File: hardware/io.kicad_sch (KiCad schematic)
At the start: 26 parts, among them J3 HALL, J4 I2C, J5 UART, J6 GPIO, J7 SWD, SW2 USER/BOOT

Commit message: Rev 0.2: 内蔵機能 (電流源/シンク・USB-PD・OPA/CMP 全モード) の活用
回路 (102/102 ネット一致):
- USB-PD シンクでモーター電源を供給: F3 → U5 LM74700 + Q10 → VBUS (PC3 で許可),
  USB VBUS 監視 (PA2), SMAJ20A。USBLC6 の基準を +3V3 に変更 (VBUS 20V 対策)
- J1 の逆接保護を U4 LM74700 + Q9 のハイサイド理想ダイオードに変更 (J1 / PD を安全に OR)
- 3 相センシングを PA5/PA6/PA7 に集約 (W 相 PA12 → PA6): CMP3 内部仮想中性点 + TIM2 捕捉
  によるセンサレス BEMF 検出, TIM2 ホール XOR, ISOURCE2 結線診断を同じピンで利用
- JP7: OPA3 入力を HB0 レッグ / バス電流で切替 (CMP2 + DAC でバス過電流・電流制限)
- JP8 + C105: QII1 (OPA1 → CMP1 → TIM3) でタコ / VR センサ / ブラシ DC 電流リップル計数
- 状態 LED を PC4 (USER/BOOT) と共用, J6/J7 を再割当 (1 線 SDI)

ファームウェア (警告 0):
- mpb.h ライブラリ: PD シンク (WCH USBPD_SNK 移植 + 8〜15V ポリシー + 給電パス制御),
  過電流保護 (CMP3/CMP2+DAC, TIM2 停止割込み), BEMF, ホール, タコ, NTC, 結線自己診断, TIM3 時間基準
- ブートローダ / テンプレートの状態 LED を PC4 (オープンドレイン) に変更

ドキュメント: docs/advanced_features.md (検討と判断, 要実機確認事項, Rev 0.3 候補)

Co-Authored-By: Claude Opus 5.5 <noreply@anthropic.com>
Claude-Session: https://claude.ai/code/session_01LENFjjhDfYjJZV1NWhB9uV
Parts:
- removed J4: I2C, Connector_JST:JST_SH_SM04B-SRSS-TB_1x04-1MP_P1.00mm_Horizontal, symbol mdrv:CONN4
- removed J5: UART, Connector_JST:JST_XH_B4B-XH-A_1x04_P2.50mm_Vertical, symbol mdrv:CONN4
- removed J7: SWD, Connector_PinHeader_2.54mm:PinHeader_1x05_P2.54mm_Vertical, symbol mdrv:CONN5
- added C105: 0.1uF, Capacitor_SMD:C_0402_1005Metric, symbol mdrv:C
- added J7: SDI, Connector_PinHeader_2.54mm:PinHeader_1x04_P2.54mm_Vertical, symbol mdrv:CONN4
- added JP8: QII_SRC, Connector_PinHeader_2.54mm:PinHeader_1x03_P2.54mm_Vertical, symbol mdrv:CONN3
- added R114: 4.7k (DNP), Resistor_SMD:R_0402_1005Metric, symbol mdrv:R
- added R123: 4.7k, Resistor_SMD:R_0402_1005Metric, symbol mdrv:R
- D3: renamed from JP6; value LED_EN -> GREEN STAT; footprint Jumper:SolderJumper-2_P1.3mm_Bridged_RoundedPad1.0x1.5mm -> LED_SMD:LED_0603_1608Metric; symbol mdrv:SJ2 -> mdrv:LED; MPN はんだジャンパ (通常ショート) -> (none)
- J4: renamed from D3; value GREEN STAT -> I2C; footprint LED_SMD:LED_0603_1608Metric -> Connector_JST:JST_SH_SM04B-SRSS-TB_1x04-1MP_P1.00mm_Horizontal; symbol mdrv:LED -> mdrv:CONN4; MPN (none) -> JST SH 4P (Qwiic/STEMMA QT 配列)
- J5: renamed from R115; value 4.7k (DNP) -> UART; footprint Resistor_SMD:R_0402_1005Metric -> Connector_JST:JST_XH_B4B-XH-A_1x04_P2.50mm_Vertical; symbol mdrv:R -> mdrv:CONN4; now fitted
- renumbered R114 to R115
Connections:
- net GPIO_PC3 is gone; now on net GPIO_PC4: J6.3 (P3)
- net +3V3: now also D3.2 (A), J4.2 (P2), J5.2 (P2), J7.1 (P1), R114.1; no longer J5.1
- net +5V: now also J6.7 (P7); no longer J6.8 (P8)
- net GND: now also J5.1 (P1), J6.8 (P8), J7.4 (P4)
- net GPIO_PC4: now also R112.2; no longer J6.4 (P4)
- net GPIO_PC5: now also J6.4 (P4); no longer J6.6 (P6)
- net I2C_SCL: now also J4.4 (P4), R115.2; no longer J5.2
- net I2C_SDA: now also J4.3 (P3), R114.2; no longer R115.2
- net SWDIO: now also J7.2 (P2)
- net UART_RX: now also J5.4 (P4)
- net UART_TX: now also J5.3 (P3)
- net nFAULT_IN: now also J6.6 (P6); no longer J6.7 (P7)
- net nRST: now also J7.3 (P3)
- net GPIO_PA6 renamed LED_STAT_K
- net LED_STAT_K: now also R112.1; no longer J6.5 (P5)
- removed net LED_STAT: D3.2, R112.1
- removed net LED_STAT_A: J4.2 (A), R112.2
- new net IBUS_F: JP8.3 (P3)
- new net QII_IN: C105.2
- new net QII_SRC: C105.1, JP8.2 (P2)
- new net TACH_IN: J6.5 (P5), R123.1
- new net TACH_R: JP8.1 (P1), R123.2
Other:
- note added: "(ブラシ DC の整流子リップル計数 = エンコーダ無し位置推定)。OPA1 出力は ADC IN19 でも読める"
- note added: "PC4: GPIO / TIM1_CH2_3 / SPI_MISO (USER/BOOT + 状態 LED 兼用, 例: DIR 入力)"
- note added: "TACH_IN → R123 → JP8 1-2 → C105 → PA12: OPA1 (AV 20/40, 自己バイアス 1.23V) → CMP1 (ヒス 100/200mV)"
- note added: "nFAULT (PA13 = TIM1_BKIN_1): Low で全ゲート OFF。10k プルアップ。3.3V 系 I/O は 5V 非耐性"
- note added: "→ TIM3 CH1 キャプチャ。ファン FG, VR センサ, 小振幅パルスの周期計測。JP8 2-3 はバス電流の AC 成分"
- note added: "汎用 GPIO 引き出し (J6) / QII1 小信号入力 (タコ・VR センサ・電流リップル)"
- note added: "温度検出 (NTC ← ISOURCE1) / USER・BOOT ボタン + 状態 LED (PC4 共用)"
- note added: "状態 LED = PC4 Low で点灯 (USER/BOOT ボタンと共用, ボタン押下中も点灯)。PA6 は 3 相センシング (W) へ。"
- note added: "通信 (I2C / UART) / デバッグ (WCH-LinkE 1 線 SDI)"
- note removed: "3.3V 系 I/O は 5V 非耐性 (絶対最大 VDD33+0.3V)。"
- note removed: "PA6 = 状態 LED。JP6 を切ると PA6 を J6 の汎用 GPIO として使える。"
- note removed: "PA6: GPIO / TIM2_CH2 / ISINK1 (状態 LED 兼用, JP6)"
- note removed: "PC3: GPIO / TIM1_CH1_3 / SPI_MOSI (例: STEP 入力)"
- note removed: "PC4: GPIO / TIM1_CH2_3 / SPI_MISO (USER/BOOT ボタン兼用, 例: DIR 入力)"
- note removed: "nFAULT (PA13 = TIM1_BKIN_1): Low で全ゲート OFF。10k プルアップ"
- note removed: "汎用 GPIO 引き出し (J6)"
- note removed: "温度検出 (パワー段近傍 NTC) / USER・BOOT ボタン / 状態 LED"
- note removed: "通信 (I2C / UART) / デバッグ (WCH-LinkE SDI)"
- moved on the sheet: D3, R112, R115

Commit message: Rev 0.3: パワー段を子基板化 (A/B/C/D) し 2 層基板レイアウトを作成
構成:
- 主基板 (60x42mm, 2 層): 右 = CH32M030 / USB-C / GPIO・I2C・UART・SDI・HALL,
  左上 = 電源 (J1 → F1 → 理想ダイオード, USB-PD 経路), 左下 = 基板間コネクタ J9/J10 (裏面)
- 子基板と裏面同士を背中合わせに重ねる (基板間 約5mm, 裏面部品は高さ 2mm 以下)。
  RESET / USER・BOOT / センシング選択は主基板 TOP、電流チャネル選択 JP5/JP7 は子基板 TOP
- 子基板 A: TPN1R603PL (既存回路) / B: TKR74F04PB (24V 系, 66x66mm) /
  C: MTN2306AN3 (廉価版) / D: MOSFET なし (全信号をピンヘッダへ引き出し)
- 基板間ピンは同じ番号同士が嵌合 (ソケットを 270° 回転して裏面実装, 座標で全 32 ピンを検証)
- コネクタは USB-C 以外すべて 2.54mm ピンヘッダ。コンデンサは 1005/1608 基本
  (入手性を確認した量産品番。50V/10uF のみ 2012)
- 24V 対応: Q9 を 40V 品 (TPN2R304PL), VHV に 47Ω + 27V ツェナー, D1/R11 の 24V 用定数を注記,
  FW は make POWER_STAGE=B で VBUS 分圧比を切替
- F1 を NANO2 10A (SMD), スイッチを B3U-1000P に小型化

基板生成 (hardware/gen_pcb.py + pcblib.py):
- 配置 → Freerouting 1.9 自動配線 → 大電流ネットのベタ化 → GND ベタ・スティッチング
  → 残り接続の補修 (格子 A*, DRC が増えない経路のみ採用) → DRC
- 5 基板とも未接続 0・電気的 DRC エラー 0 (警告はシルクの重なりのみ)
- 製造データ hardware/fab/*.zip (ガーバー, ドリル, 両面の部品座標)

回路図: 主基板 82/82, 子基板 A/B/C 41/41, D 21/21 ネット一致。FW は A/B とも警告 0 でビルド。

Co-Authored-By: Claude Opus 5.5 <noreply@anthropic.com>
Claude-Session: https://claude.ai/code/session_01LENFjjhDfYjJZV1NWhB9uV
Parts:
- removed TH1: 10k B3435, Resistor_SMD:R_0402_1005Metric, symbol mdrv:NTC
- C100, C101, C102: value 1nF -> 1nF/50V; MPN (none) -> Murata GRM155R71H102KA01D (X7R 1005)
- C103, C105: value 0.1uF -> 0.1uF/50V; MPN (none) -> Murata GRM155R71H104KE14D (X7R 1005)
- J3: footprint Connector_JST:JST_XH_B5B-XH-A_1x05_P2.50mm_Vertical -> Connector_PinHeader_2.54mm:PinHeader_1x05_P2.54mm_Vertical; MPN (none) -> 2.54mm 1x5 ピンヘッダ
- J4: footprint Connector_JST:JST_SH_SM04B-SRSS-TB_1x04-1MP_P1.00mm_Horizontal -> Connector_PinHeader_2.54mm:PinHeader_1x04_P2.54mm_Vertical; MPN JST SH 4P (Qwiic/STEMMA QT 配列) -> 2.54mm 1x4 ピンヘッダ (Qwiic/STEMMA QT と同じ並び)
- J5: footprint Connector_JST:JST_XH_B4B-XH-A_1x04_P2.50mm_Vertical -> Connector_PinHeader_2.54mm:PinHeader_1x04_P2.54mm_Vertical; MPN (none) -> 2.54mm 1x4 ピンヘッダ
- J6: MPN 2.54mm 8P ピンヘッダ -> 2.54mm 1x8 ピンヘッダ
- J7: MPN 2.54mm 4P (WCH-LinkE 1 線 SDI: 3V3/SWIO/RST/GND) -> 2.54mm 1x4 ピンヘッダ (WCH-LinkE 1 線 SDI: 3V3/SWIO/RST/GND)
- SW2: footprint Button_Switch_SMD:SW_SPST_TL3342 -> Button_Switch_SMD:SW_SPST_B3U-1000P; MPN (none) -> Omron B3U-1000P (3x2.5mm SMD タクト, 上押し)
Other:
- note added: "TACH_IN → R123 → JP8 1-2 → C105 → PA12: OPA1 (AV 20/40, 自己バイアス 1.23V) → CMP1 → TIM3 CH1"
- note added: "ファン FG, VR センサ, 小振幅パルスの周期計測。JP8 2-3 はバス電流の AC 成分 (ブラシ DC リップル計数)"
- note added: "ホールセンサ入力 (J3 ピンヘッダ)"
- note added: "温度検出 (NTC は子基板) / USER・BOOT ボタン + 状態 LED (PC4 共用)"
- note added: "状態 LED = PC4 Low で点灯 (USER/BOOT ボタンと共用, ボタン押下中も点灯)。"
- note removed: "(ブラシ DC の整流子リップル計数 = エンコーダ無し位置推定)。OPA1 出力は ADC IN19 でも読める"
- note removed: "TACH_IN → R123 → JP8 1-2 → C105 → PA12: OPA1 (AV 20/40, 自己バイアス 1.23V) → CMP1 (ヒス 100/200mV)"
- note removed: "→ TIM3 CH1 キャプチャ。ファン FG, VR センサ, 小振幅パルスの周期計測。JP8 2-3 はバス電流の AC 成分"
- note removed: "ホールセンサ入力 (オープンコレクタ想定)"
- note removed: "温度検出 (NTC ← ISOURCE1) / USER・BOOT ボタン + 状態 LED (PC4 共用)"
- note removed: "状態 LED = PC4 Low で点灯 (USER/BOOT ボタンと共用, ボタン押下中も点灯)。PA6 は 3 相センシング (W) へ。"
- title: mPBCH32M030DS0  CH32M030 Universal Motor Driver -> mPBCH32M030DS0  CH32M030 Universal Motor Driver - Main board

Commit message: Rev 0.4: DIP-42 MCU module + power boards A/B/C (KiCad 8)
- MCU module: 20.32 x 53.34mm (8 x 21 grid), DIP-42 (0.6in rows), fits
  an 82 x 52mm breadboard. Headers can be fitted from either side;
  signal names on bottom silk. All LEDs (power, status, 8 gate LEDs) on
  the module top.
- Power boards take the module in two 1x21 sockets (left/right
  symmetric mating). FETs/shunts on the heatsink side, no LEDs.
  Voltage-dependent parts (TVS, OVP divider, bulk caps, BEMF divider)
  moved to the power boards. Breakout board D removed.
  A/C: 20.32 x 71.94mm, B (TO-263 x8): 40.64 x 66.94mm.
- Capacitors re-selected for realistic size vs voltage/capacitance
  (4.7uF 1608, 10uF/25V 2012, 10uF/50V 1206, 4.7nF/100V 1608, low
  profile electrolytics).
- Schematics and boards generated in KiCad 8 format; netlists verified
  with KiCad 8.0.9.
- Layout pipeline: Freerouting bridge (parallel), second pass, early
  repair before pours, island-aware maze repair, DRC via kicad-cli.
- DRC: power boards A/B/C have 0 unconnected / 0 electrical errors.
  The MCU module still has unrouted connections (work in progress).

Co-Authored-By: Claude Opus 5.5 <noreply@anthropic.com>
Claude-Session: https://claude.ai/code/session_01LENFjjhDfYjJZV1NWhB9uV
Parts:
- removed J3: HALL, Connector_PinHeader_2.54mm:PinHeader_1x05_P2.54mm_Vertical, symbol mdrv:CONN5
- removed J4: I2C, Connector_PinHeader_2.54mm:PinHeader_1x04_P2.54mm_Vertical, symbol mdrv:CONN4
- removed J5: UART, Connector_PinHeader_2.54mm:PinHeader_1x04_P2.54mm_Vertical, symbol mdrv:CONN4
- removed J6: GPIO, Connector_PinHeader_2.54mm:PinHeader_1x08_P2.54mm_Vertical, symbol mdrv:CONN8
- removed J7: SDI, Connector_PinHeader_2.54mm:PinHeader_1x04_P2.54mm_Vertical, symbol mdrv:CONN4
- added D10: RED GH0, LED_SMD:LED_0402_1005Metric, symbol mdrv:LED
- added D11: GREEN GL0, LED_SMD:LED_0402_1005Metric, symbol mdrv:LED
- added D12: RED GH1, LED_SMD:LED_0402_1005Metric, symbol mdrv:LED
- added D13: GREEN GL1, LED_SMD:LED_0402_1005Metric, symbol mdrv:LED
- added D14: RED GH2, LED_SMD:LED_0402_1005Metric, symbol mdrv:LED
- added D17: GREEN GL3, LED_SMD:LED_0402_1005Metric, symbol mdrv:LED
- added J1: EDGE_L, Connector_PinHeader_2.54mm:PinHeader_1x21_P2.54mm_Vertical, symbol mdrv:CONN21
- added JP2: SEL_U, Jumper:SolderJumper-3_P1.3mm_Bridged12_RoundedPad1.0x1.5mm_NumberLabels, symbol mdrv:SJ3
- added JP3: SEL_V, Jumper:SolderJumper-3_P1.3mm_Bridged12_RoundedPad1.0x1.5mm_NumberLabels, symbol mdrv:SJ3
- added JP4: SEL_W, Jumper:SolderJumper-3_P1.3mm_Bridged12_RoundedPad1.0x1.5mm_NumberLabels, symbol mdrv:SJ3
- added JP8: QII_SRC, Jumper:SolderJumper-3_P1.3mm_Bridged12_RoundedPad1.0x1.5mm_NumberLabels, symbol mdrv:SJ3
- added R106, R123: 4.7k, Resistor_SMD:R_0402_1005Metric, symbol mdrv:R
- added R120: 470R, Resistor_SMD:R_0402_1005Metric, symbol mdrv:R
- added R122: 10k, Resistor_SMD:R_0402_1005Metric, symbol mdrv:R
- added R50, R51, R52, R53, R54, R55: 22k, Resistor_SMD:R_0402_1005Metric, symbol mdrv:R
- D15: renamed from R120; value 470R -> GREEN GL2; footprint Resistor_SMD:R_0402_1005Metric -> LED_SMD:LED_0402_1005Metric; symbol mdrv:R -> mdrv:LED; MPN (none) -> 1005 チップ LED (例: Kingbright APHHS1005)
- D16: renamed from R123; value 4.7k -> RED GH3; footprint Resistor_SMD:R_0402_1005Metric -> LED_SMD:LED_0402_1005Metric; symbol mdrv:R -> mdrv:LED; MPN (none) -> 1005 チップ LED (例: Kingbright APHHS1005)
- D3: MPN (none) -> 1608 チップ LED
- J2: renamed from R106; value 4.7k -> EDGE_R; footprint Resistor_SMD:R_0402_1005Metric -> Connector_PinHeader_2.54mm:PinHeader_1x21_P2.54mm_Vertical; symbol mdrv:R -> mdrv:CONN21; MPN (none) -> 2.54mm 1x21 ピンヘッダ (裏 or 表から実装)
- R56: renamed from R122; value 10k -> 22k
- R57: renamed from JP8; value QII_SRC -> 22k; footprint Connector_PinHeader_2.54mm:PinHeader_1x03_P2.54mm_Vertical -> Resistor_SMD:R_0402_1005Metric; symbol mdrv:CONN3 -> mdrv:R; MPN 2.54mm 3P + ジャンパ (1-2: TACH_IN / 2-3: バス電流リップル) -> (none)
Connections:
- net +3V3: now also J1.6 (P6), R106.2, R122.1; no longer J2.2, R56.1
- net +5V: now also J1.5 (P5)
- net GND: now also D15.1 (K), J2.1 (P1), J2.21 (P21), D11.1 (K), D13.1 (K), D17.1 (K), J1.21 (P21)
- net GPIO_PC4: now also J2.4 (P4)
- net GPIO_PC5: now also J2.5 (P5)
- net HALL_A: now also JP2.3
- net HALL_A_IN: now also J1.14 (P14)
- net HALL_B: now also JP3.3
- net HALL_B_IN: now also J1.15 (P15)
- net HALL_C: now also JP4.3
- net HALL_C_IN: now also J1.16 (P16), R106.1; no longer J2.1
- net I2C_SCL: now also J2.19 (P19)
- net I2C_SDA: now also J2.18 (P18)
- net IBUS_F: now also JP8.3; no longer R57.3 (P3)
- net NTC: now also J1.10 (P10)
- net QII_SRC: now also JP8.2; no longer R57.2 (P2)
- net SWDIO: now also J1.7 (P7)
- net TACH_IN: now also J1.20 (P20), R123.1; no longer D16.1
- net TACH_R: now also JP8.1, R123.2; no longer D16.2, R57.1 (P1)
- net UART_RX: now also J2.3 (P3)
- net UART_TX: now also J2.2 (P2)
- net nFAULT: now also R120.2, R122.2; no longer D15.2, R56.2
- net nFAULT_IN: now also J2.20 (P20), R120.1; no longer D15.1
- net nRST: now also J1.8 (P8)
- new net BEMF_U: J1.11 (P11), JP2.1
- new net BEMF_V: J1.12 (P12), JP3.1
- new net BEMF_W: J1.13 (P13), JP4.1
- new net GLEDH0: D10.2 (A), R50.2
- new net GLEDH1: D12.2 (A), R52.2
- new net GLEDH2: D14.2 (A), R54.2
- new net GLEDH3: D16.2 (A), R56.2
- new net GLEDL0: D11.2 (A), R51.2
- new net GLEDL1: D13.2 (A), R53.2
- new net GLEDL2: D15.2 (A), R55.2
- new net GLEDL3: D17.2 (A), R57.2
- new net HO0: J2.15 (P15), R50.1
- new net HO1: J2.12 (P12), R52.1
- new net HO2: J2.9 (P9), R54.1
- new net HO3: J2.6 (P6), R56.1
- new net ISA_SEL: J1.17 (P17)
- new net ISB_SEL: J1.19 (P19)
- new net ISH: J1.18 (P18)
- new net LO0: J2.17 (P17), R51.1
- new net LO1: J2.14 (P14), R53.1
- new net LO2: J2.11 (P11), R55.1
- new net LO3: J2.8 (P8), R57.1
- new net PD_PWR_EN: J1.4 (P4)
- new net SENS_U: JP2.2
- new net SENS_V: JP3.2
- new net SENS_W: JP4.2
- new net SW0: D10.1 (K), J2.16 (P16)
- new net SW1: D12.1 (K), J2.13 (P13)
- new net SW2: D14.1 (K), J2.10 (P10)
- new net SW3: D16.1 (K), J2.7 (P7)
- new net USB_VBUS: J1.1 (P1), J1.2 (P2)
- new net VBUS: J1.9 (P9)
- new net VBUS_SNS: J1.3 (P3)
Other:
- note added: "3 相センシング選択 (はんだジャンパ, 出荷時 1-2 = 相電圧) / QII 入力選択"
- note added: "DIP 端子 (2.54mm, 21 ピン x 2 列, 列間 15.24mm)"
- note added: "H: HOx-SWx (ハイサイドのゲート電圧), L: LOx-GND。約 0.35mA @ VDD8=10V。PWM のデューティで明るさが変わる。"
- note added: "NTC 本体は子基板 (MOSFET 近傍)。PA4 の ISOURCE1 で駆動。I2C プルアップ R114/R115 は必要時のみ。"
- note added: "ゲート確認 LED (モジュール上面に 8 個: 子基板の部品面はヒートシンク側で見えないため)"
- note added: "ホール入力 / USER・BOOT + 状態 LED / I2C / nFAULT / NTC"
- note added: "子基板は同じピン番号のソケット (左右対称) で受ける。"
- note added: "子基板を付けずブレッドボードで使うときも同じ: BEMF_x / HALL_x_IN ピンに信号を入れる。"
- note removed: "I2C プルアップはバスに 1 組。マスタ側に無い場合のみ R114/R115 を実装。"
- note removed: "J7 の 3V3 は電圧参照用。WCH-Link から 3.3V を供給しないこと (VDD33 ≤ VDD8 ≤ VHV の制約)。"
- note removed: "NTC は PA4 (ISOURCE1 内蔵電流源) → ADC_IN5。R110 (DNP) で分圧方式にも変更可。"
- note removed: "PC4: GPIO / TIM1_CH2_3 / SPI_MISO (USER/BOOT + 状態 LED 兼用, 例: DIR 入力)"
- note removed: "PC5: HV I/O (VHV 系, 入力耐圧 VHV+6V, 出力 ≈1mA) → 12V 系の EN / リミット入力に"
- note removed: "TACH_IN → R123 → JP8 1-2 → C105 → PA12: OPA1 (AV 20/40, 自己バイアス 1.23V) → CMP1 → TIM3 CH1"
- note removed: "nFAULT (PA13 = TIM1_BKIN_1): Low で全ゲート OFF。10k プルアップ。3.3V 系 I/O は 5V 非耐性"
- note removed: "ファン FG, VR センサ, 小振幅パルスの周期計測。JP8 2-3 はバス電流の AC 成分 (ブラシ DC リップル計数)"
- note removed: "プルアップは 3.3V (MCU 入力保護)。5V プッシュプル出力のホールは 1k 直列で電流制限 (注入 ≤4mA)。"
- note removed: "ホールセンサ入力 (J3 ピンヘッダ)"
- note removed: "汎用 GPIO 引き出し (J6) / QII1 小信号入力 (タコ・VR センサ・電流リップル)"
- note removed: "温度検出 (NTC は子基板) / USER・BOOT ボタン + 状態 LED (PC4 共用)"
- note removed: "状態 LED = PC4 Low で点灯 (USER/BOOT ボタンと共用, ボタン押下中も点灯)。"
- note removed: "通信 (I2C / UART) / デバッグ (WCH-LinkE 1 線 SDI)"
- title: mPBCH32M030DS0  CH32M030 Universal Motor Driver - Main board -> mPBCH32M030DS0  CH32M030 motor-driver MCU module (DIP-42)
- moved on the sheet: R56

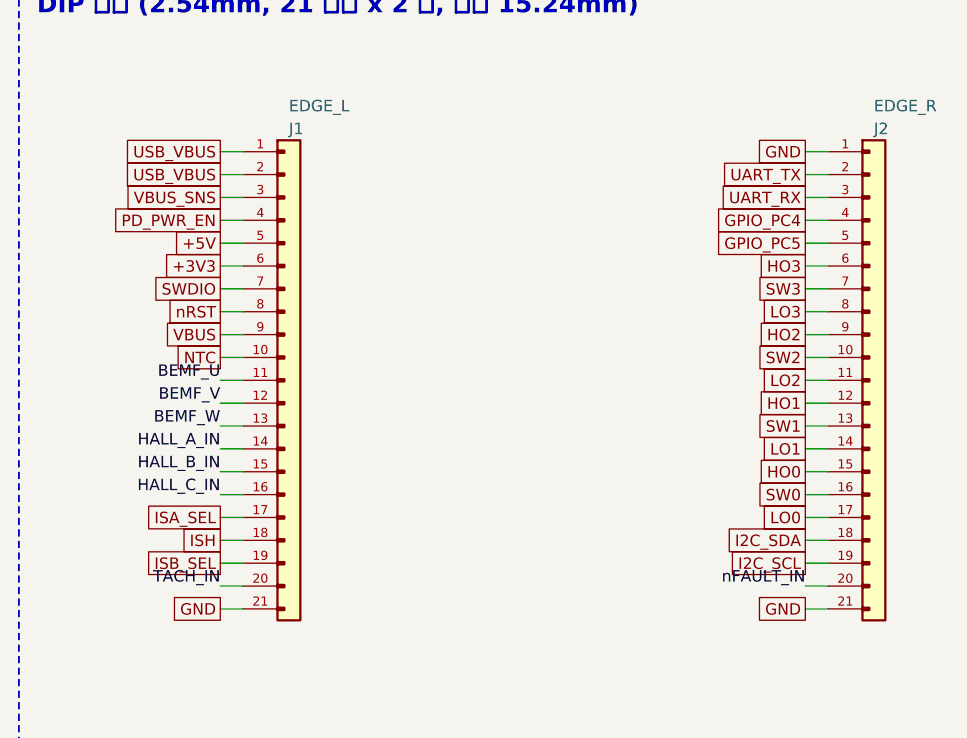
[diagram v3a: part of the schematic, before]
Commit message: Rev 0.4: rework module pinout for routability, power boards regenerated
- Module edge pin order follows the CH32M030 QFN48 pin sides so the
  breakout traces nest instead of crossing (J1: USB_VBUS, PD_PWR_EN,
  PC4/PC5, +3V3, +5V, SWDIO, VBUS, NTC, BEMF, HALL, ISx, TACH;
  J2: RX/TX, nRST, gate drive HO3..LO0, VBUS_SNS, I2C, nFAULT).
- Module: area under the QFN kept for fan-out (filters and the VHV/USB
  diode block moved away, gate LEDs right-aligned to J2).
- Power boards A/B/C re-placed for the new pinout (VBUS divider next to
  J2 VBUS_SNS, LM74700 next to its FET) and re-routed: all three at
  0 unconnected / 0 electrical DRC errors.
- Layout tooling: DRC via kicad-cli in a separate process, reload after
  SES import, selectable Freerouting jar, optional rip-up repair,
  configurable Freerouting timeout.
- MCU module still has unrouted connections (work in progress).

Co-Authored-By: Claude Opus 5.5 <noreply@anthropic.com>
Claude-Session: https://claude.ai/code/session_01LENFjjhDfYjJZV1NWhB9uV
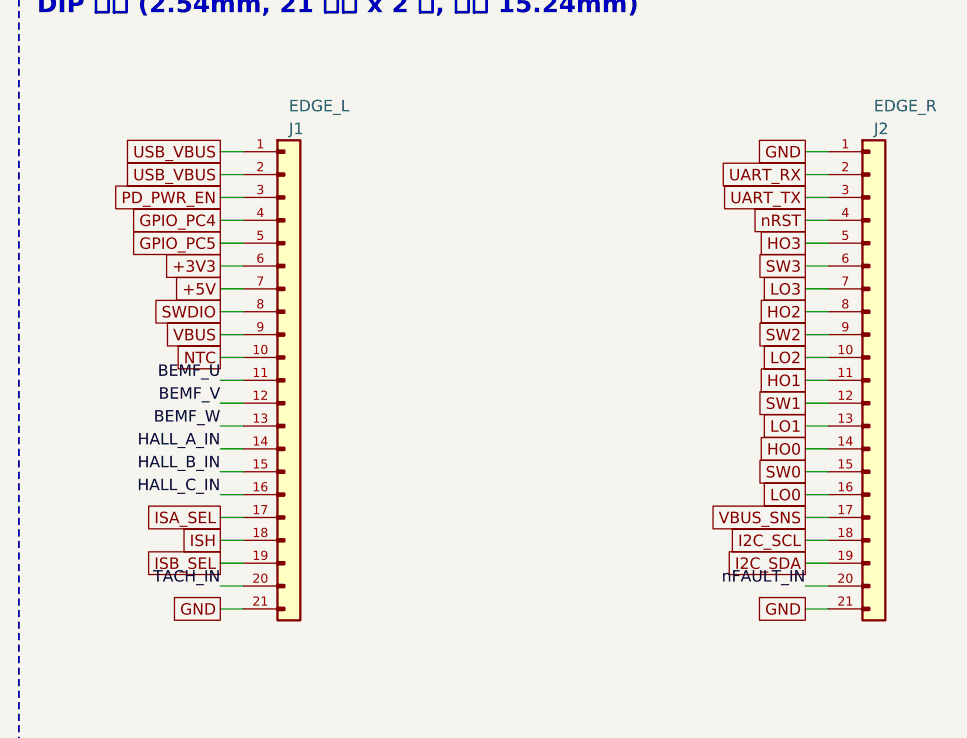
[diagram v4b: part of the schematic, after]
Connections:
- net +5V: now also J1.7 (P7); no longer J1.5 (P5)
- net GPIO_PC4: now also J1.4 (P4); no longer J2.4 (P4)
- net GPIO_PC5: now also J1.5 (P5); no longer J2.5 (P5)
- net HO0: now also J2.14 (P14); no longer J2.15 (P15)
- net HO1: now also J2.11 (P11); no longer J2.12 (P12)
- net HO2: now also J2.8 (P8); no longer J2.9 (P9)
- net HO3: now also J2.5 (P5); no longer J2.6 (P6)
- net I2C_SCL: now also J2.18 (P18); no longer J2.19 (P19)
- net I2C_SDA: now also J2.19 (P19); no longer J2.18 (P18)
- net LO0: now also J2.16 (P16); no longer J2.17 (P17)
- net LO1: now also J2.13 (P13); no longer J2.14 (P14)
- net LO2: now also J2.10 (P10); no longer J2.11 (P11)
- net LO3: now also J2.7 (P7); no longer J2.8 (P8)
- net PD_PWR_EN: now also J1.3 (P3); no longer J1.4 (P4)
- net SW0: now also J2.15 (P15); no longer J2.16 (P16)
- net SW1: now also J2.12 (P12); no longer J2.13 (P13)
- net SW2: now also J2.9 (P9); no longer J2.10 (P10)
- net SW3: now also J2.6 (P6); no longer J2.7 (P7)
- net SWDIO: now also J1.8 (P8); no longer J1.7 (P7)
- net UART_RX: now also J2.2 (P2); no longer J2.3 (P3)
- net UART_TX: now also J2.3 (P3); no longer J2.2 (P2)
- net VBUS_SNS: now also J2.17 (P17); no longer J1.3 (P3)
- net nRST: now also J2.4 (P4); no longer J1.8 (P8)
